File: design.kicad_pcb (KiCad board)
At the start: 2 copper layers, 28.5 x 12 mm, 7 parts, among them J1 USB_C_Receptacle, J2 Conn_01x05, U1 ATtiny1616-M

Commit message: remove template stuff
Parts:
- removed C1, C2: C_Small, Capacitor_SMD:C_0805_2012Metric
- removed D1: LED, LED_THT:LED_D5.0mm_FlatTop
- removed D2: LED, LED_SMD:LED_0603_1608Metric_Pad1.05x0.95mm_HandSolder
- removed J1: USB_C_Receptacle, Connector_USB:USB_C_Receptacle_HRO_TYPE-C-31-M-12
- removed J2: Conn_01x05, E32-xxxT20D:UDPI_interface
- removed U1: ATtiny1616-M, Package_DFN_QFN:VQFN-20-1EP_3x3mm_P0.4mm_EP1.7x1.7mm
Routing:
- removed copper zone on F.Cu, net Net-(J1-PadA1)
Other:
- board outline removed
- net class Default removed
- board text removed: "<<ID>>"
- board text removed: "<<date>>"
- board text removed: "<<hash>>"
- board text removed: "<<project_name>>"
- board text removed: "<<version>>"

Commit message: add TPS61099
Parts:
- added U1: TPS61099YFFT, Converter_DCDC_custom:BGA6N40P3X2_122X88X62N, F.Cu at (147.0, 96.0)
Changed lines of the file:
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@@
   )
   (net 0 "")
+  (net 1 "unconnected-(U1-PadA1)")
+  (net 2 "unconnected-(U1-PadA2)")
+  (net 3 "unconnected-(U1-PadB1)")
+  (net 4 "unconnected-(U1-PadB2)")
+  (net 5 "unconnected-(U1-PadC1)")
+  (net 6 "unconnected-(U1-PadC2)")
+  (footprint "Converter_DCDC_custom:BGA6N40P3X2_122X88X62N" (layer "F.Cu")
+    (at 147 96)
+    (property "MANUFACTURER" "Texas Instruments")
+    (property "MAXIMUM_PACKAGE_HEIGHT" "0.625mm")
+    (property "PARTREV" "K")
+    (property "STANDARD" "IPC 7351B")
+    (property "Sheetfile" "design.kicad_sch")
+    (property "Sheetname" "")
+    (attr through_hole)
+    (fp_text reference "U1" (at 0.082 -1.9178) (layer "F.SilkS")
+      (effects (font (size 0.48 0.48) (thickness 0.15)))
+    )
+    (fp_text value "TPS61099YFFT" (at 5.2636 1.9178) (layer "F.Fab")
+      (effects (font (size 0.48 0.48) (thickness 0.15)))
+    )
+    (fp_line (start -0.645 0.845) (end -0.645 0.4225) (layer "F.SilkS") (width 0.127))
+    (fp_line (start -0.645 -0.845) (end -0.645 -0.4225) (layer "F.SilkS") (width 0.127))
+    (fp_line (start 0.645 -0.845) (end 0.645 -0.4225) (layer "F.SilkS") (width 0.127))
+    (fp_line (start 0.645 0.845) (end 0.645 0.4225) (layer "F.SilkS") (width 0.127))
+    (fp_line (start 0.645 0.845) (end 0.3225 0.845) (layer "F.SilkS") (width 0.127))
+    (fp_line (start -0.645 0.845) (end -0.3225 0.845) (layer "F.SilkS") (width 0.127))
+    (fp_line (start -0.645 -0.845) (end -0.3225 -0.845) (layer "F.SilkS") (width 0.127))
+    (fp_line (start 0.645 -0.845) (end 0.3225 -0.845) (layer "F.SilkS") (width 0.127))
+    (fp_circle (center -0.942 -0.4) (end -0.842 -0.4) (layer "F.SilkS") (width 0.2) (fill none))
+    (fp_line (start -1.442 1.613) (end -1.442 -1.613) (layer "F.CrtYd") (width 0.05))
+    (fp_line (start -1.442 -1.613) (end 1.442 -1.613) (layer "F.CrtYd") (width 0.05))
+    (fp_line (start -1.442 1.613) (end 1.442 1.613) (layer "F.CrtYd") (width 0.05))
+    (fp_line (start 1.442 1.613) (end 1.442 -1.613) (layer "F.CrtYd") (width 0.05))
+    (fp_line (start 0.442 0.613) (end -0.442 0.613) (layer "F.Fab") (width 0.127))
+    (fp_line (start -0.442 0.613) (end -0.442 -0.613) (layer "F.Fab") (width 0.127))
+    (fp_line (start 0.442 -0.613) (end -0.442 -0.613) (layer "F.Fab") (width 0.127))
+    (fp_line (start 0.442 0.613) (end 0.442 -0.613) (layer "F.Fab") (width 0.127))
+    (fp_circle (center -0.942 -0.4) (end -0.842 -0.4) (layer "F.Fab") (width 0.2) (fill none))
+    (pad "A1" smd circle (at -0.2 -0.4) (size 0.25 0.25) (layers "F.Cu" "F.Paste" "F.Mask")
+      (net 1 "unconnected-(U1-PadA1)") (pinfunction "VIN") (pintype "input"))
+    (pad "A2" smd circle (at 0.2 -0.4) (size 0.25 0.25) (layers "F.Cu" "F.Paste" "F.Mask")
+      (net 2 "unconnected-(U1-PadA2)") (pinfunction "GND") (pintype "power_in"))
+    (pad "B1" smd circle (at -0.2 0) (size 0.25 0.25) (layers "F.Cu" "F.Paste" "F.Mask")
+      (net 3 "unconnected-(U1-PadB1)") (pinfunction "SW") (pintype "passive"))
+    (pad "B2" smd circle (at 0.2 0) (size 0.25 0.25) (layers "F.Cu" "F.Paste" "F.Mask")
+      (net 4 "unconnected-(U1-PadB2)") (pinfunction "VOUT") (pintype "output"))
+    (pad "C1" smd circle (at -0.2 0.4) (size 0.25 0.25) (layers "F.Cu" "F.Paste" "F.Mask")
+      (net 5 "unconnected-(U1-PadC1)") (pinfunction "EN") (pintype "input"))
+    (pad "C2" smd circle (at 0.2 0.4) (size 0.25 0.25) (layers "F.Cu" "F.Paste" "F.Mask")
+      (net 6 "unconnected-(U1-PadC2)") (pinfunction "FB") (pintype "input"))
+    (model "/Users/tobias/Documents/GitHub/ki-lib/3D/Converter_DCDC.3dshapes/TPS61099xYFFT.step"
+      (offset (xyz 0 0 0))
+      (scale (xyz 1 1 1))
+      (rotate (xyz -90 0 0))
+    )
+  )
 )

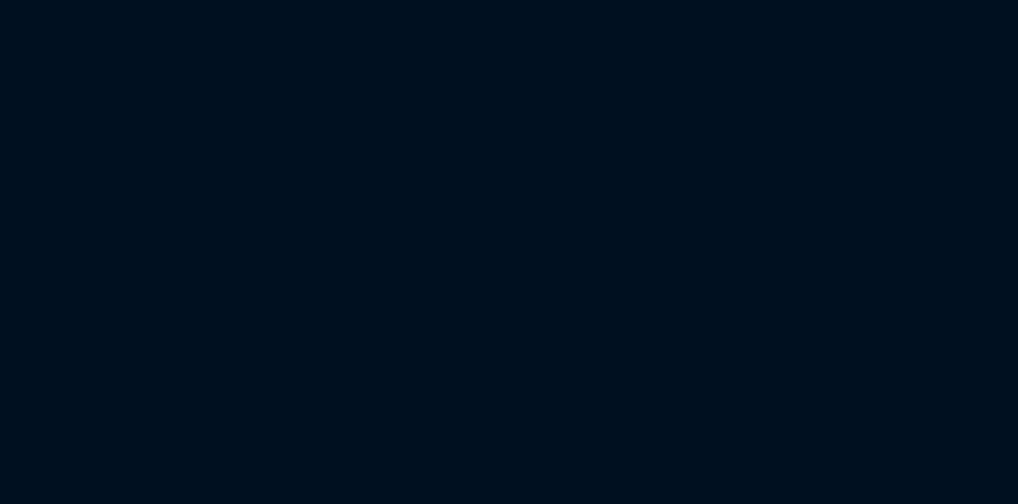
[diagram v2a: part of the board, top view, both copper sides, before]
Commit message: PCB Add variables
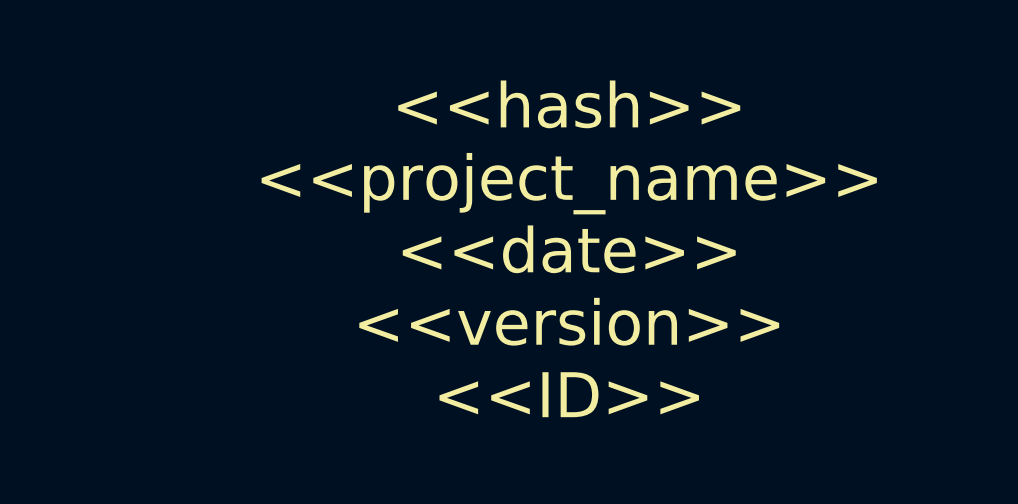
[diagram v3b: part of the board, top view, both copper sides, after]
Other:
- board text added: "<<hash>> <<project_name>> <<date>> <<version>> <<ID>>"
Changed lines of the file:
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@@
     )
   )
+  (gr_text "<<hash>>\n<<project_name>>\n<<date>>\n<<version>>\n<<ID>>" (at 169 94) (layer "F.SilkS")
+    (effects (font (size 1.5 1.5) (thickness 0.3)))
+  )
 )

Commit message: remove date variable
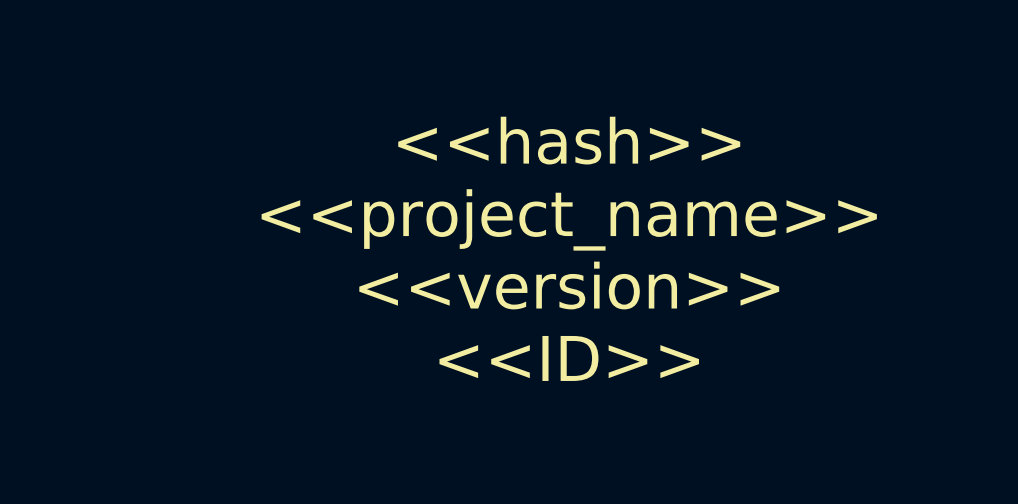
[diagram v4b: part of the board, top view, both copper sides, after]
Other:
- board text added: "<<hash>> <<project_name>> <<version>> <<ID>>"
- board text removed: "<<hash>> <<project_name>> <<date>> <<version>> <<ID>>"
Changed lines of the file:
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@@
   (title_block
     (title "<<project_name>>")
-    (date "<<date>>")
     (rev "<<version>>")
     (comment 4 "<<hash>>")
@@
     )
   )
-  (gr_text "<<hash>>\n<<project_name>>\n<<date>>\n<<version>>\n<<ID>>" (at 169 94) (layer "F.SilkS")
+  (gr_text "<<hash>>\n<<project_name>>\n<<version>>\n<<ID>>" (at 169 94) (layer "F.SilkS")
     (effects (font (size 1.5 1.5) (thickness 0.3)))
   )
